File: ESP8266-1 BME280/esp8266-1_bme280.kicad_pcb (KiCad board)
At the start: 2 copper layers, 21.6 x 15.6 mm, 11 parts, among them J1 USB_B_Micro, J2 Conn_02x04_Odd_Even, U1 AMS1117-3.3, U2 BME280

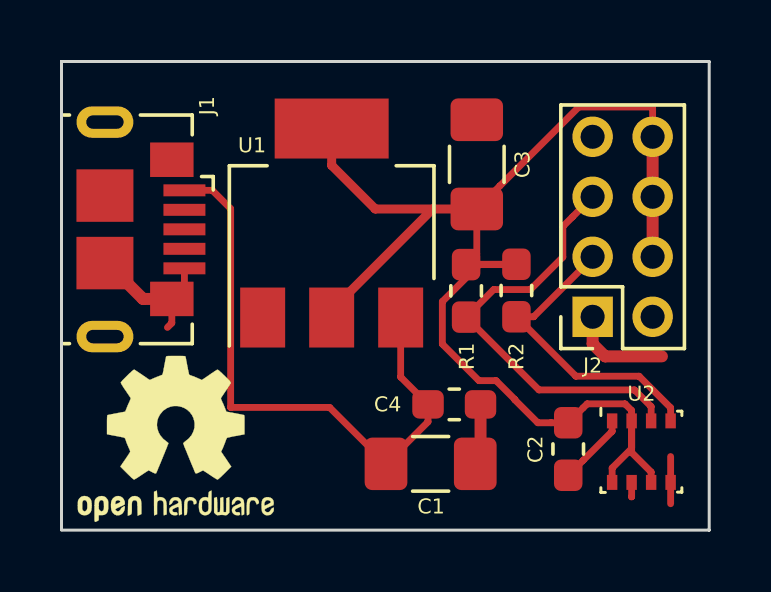
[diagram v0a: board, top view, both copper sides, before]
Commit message: Add mounting hole, add BME280 3D modell
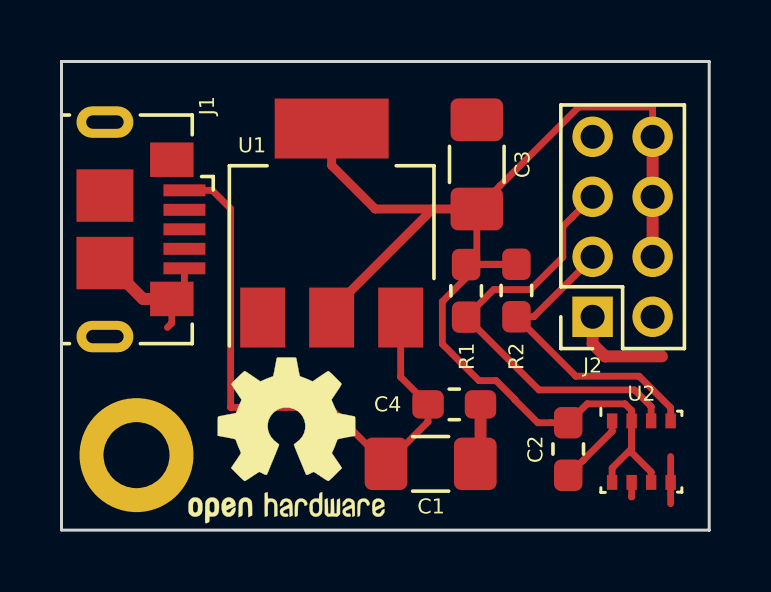
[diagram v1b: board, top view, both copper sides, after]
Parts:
- added H1: MountingHole, MountingHole:MountingHole_2.2mm_M2_DIN965_Pad, F.Cu at (112.7, 98.9)
- moved REF** 3.69 mm to (117.7, 98.4)
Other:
- board text added: "ESP8266-1 BME280 Board Revision 2 - 02/2019 github.com/elnappo/PCB"
- board text removed: "ESP8266-1 BME280 Board Revision v0.1.0 - 01/2019 github.com/elnappo/PCB"
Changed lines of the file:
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@@
     (tracks 93)
     (zones 0)
-    (modules 11)
+    (modules 12)
     (nets 6)
   )
@@
   (layers
     (0 F.Cu signal)
-    (31 B.Cu signal hide)
+    (31 B.Cu signal)
     (32 B.Adhes user)
     (33 F.Adhes user)
@@
     (last_trace_width 0.2286)
     (trace_clearance 0.2032)
-    (zone_clearance 0.4)
+    (zone_clearance 0.1)
     (zone_45_only no)
     (trace_min 0.22)
@@
       (viasonmask false)
       (mode 1)
-      (useauxorigin false)
+      (useauxorigin true)
       (hpglpennumber 1)
       (hpglpenspeed 20)
@@
       (psa4output false)
       (plotreference true)
-      (plotvalue true)
+      (plotvalue false)
       (plotinvisibletext false)
       (padsonsilk false)
@@
       (outputformat 1)
       (mirror false)
-      (drillshape 1)
+      (drillshape 0)
       (scaleselection 1)
-      (outputdirectory ""))
+      (outputdirectory "Gerber/"))
   )
   (net 0 "")
@@
       (rotate (xyz 0 0 0))
     )
+    (model /Users/elnappo/Coding/KiCad/libs/3d/BME280--3DModel-STEP-56544.STEP
+      (at (xyz 0 0 0))
+      (scale (xyz 1 1 1))
+      (rotate (xyz -90 0 0))
+    )
   )
   (module Capacitor_SMD:C_0603_1608Metric_Pad1.05x0.95mm_HandSolder (layer F.Cu)
@@
   )
   (module Symbol:OSHW-Logo2_7.3x6mm_SilkScreen (layer F.Cu)
-    (at 114.046 98.3996)
+    (at 117.736 98.4476)
     (descr "Open Source Hardware Symbol")
     (tags "Logo Symbol OSHW")
@@
       (xy -2.549664 1.91989) (xy -2.469928 1.911165) (xy -2.400256 1.919918)) (layer F.SilkS) (width 0.01))
   )
-  (gr_text "ESP8266-1 BME280 Board\nRevision v0.1.0 - 01/2019\ngithub.com/elnappo/PCB" (at 130.8354 98.0694) (layer B.SilkS)
-    (effects (font (size 0.508 0.508) (thickness 0.127)) (justify left mirror))
+  (module MountingHole:MountingHole_2.2mm_M2_DIN965_Pad (layer F.Cu)
+    (at 112.736 98.9476)
+    (descr "Mounting Hole 2.2mm, M2, DIN965")
+    (tags "mounting hole 2.2mm m2 din965")
+    (attr virtual)
+    (fp_text reference H1 (at 0 -2.9) (layer F.SilkS) hide
+      (effects (font (size 1 1) (thickness 0.15)))
+    )
+    (fp_text value MountingHole (at 0 2.9) (layer F.Fab)
+      (effects (font (size 1 1) (thickness 0.15)))
+    )
+    (fp_text user %R (at 0.3 0) (layer F.Fab)
+      (effects (font (size 1 1) (thickness 0.15)))
+    )
+    (fp_circle (center 0 0) (end 1.9 0) (layer Cmts.User) (width 0.15))
+    (fp_circle (center 0 0) (end 2.15 0) (layer F.CrtYd) (width 0.05))
+    (pad 1 thru_hole circle (at 0 0) (size 3.8 3.8) (drill 2.2) (layers *.Cu *.Mask))
+  )
+  (gr_text "ESP8266-1 BME280 Board\nRevision 2 - 02/2019\ngithub.com/elnappo/PCB" (at 130.8354 98.0694) (layer B.SilkS)
+    (effects (font (size 0.75 0.75) (thickness 0.15)) (justify left mirror))
   )
   (gr_line (start 110.236 85.8266) (end 131.826 85.8266) (layer Edge.Cuts) (width 0.1))
@@
   (segment (start 129.8904 97.8064) (end 129.8904 97.3278) (width 0.2286) (layer F.Cu) (net 5) (status 10))
   (zone (net 1) (net_name GND) (layer F.Cu) (hatch edge 0.508)
-    (connect_pads (clearance 0.4))
+    (connect_pads (clearance 0.1))
     (min_thickness 0.254)
     (fill yes (arc_segments 32) (thermal_gap 0.4) (thermal_bridge_width 0.5) (smoothing chamfer))
@@
   )
   (zone (net 1) (net_name GND) (layer B.Cu) (hatch edge 0.508)
-    (connect_pads yes (clearance 0.4))
+    (connect_pads yes (clearance 0.1))
     (min_thickness 0.254)
     (fill yes (arc_segments 32) (thermal_gap 0.4) (thermal_bridge_width 0.508) (smoothing chamfer))
